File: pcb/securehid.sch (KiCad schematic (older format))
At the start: 194 parts, among them J1 USB_B_Micro, J2 SWD_HOST, J3 UART_HOST, J4 SWD_DEVICE, J5 UART_DEVICE, J6 USB_A, J7 USB_SPARE, J8 USB_A, Q1 AO3400, Q2 AO3400, Q3 AO3400, SW1 SW_Push, U1 AP1117-33, U2 STM32F103C8T6, U3 STM32F407VET6, U4 FE1.1s, U5 AP1117-33, Y1 8MHz, Y2 8MHz, Y3 32.768kHz, Y4 12MHz

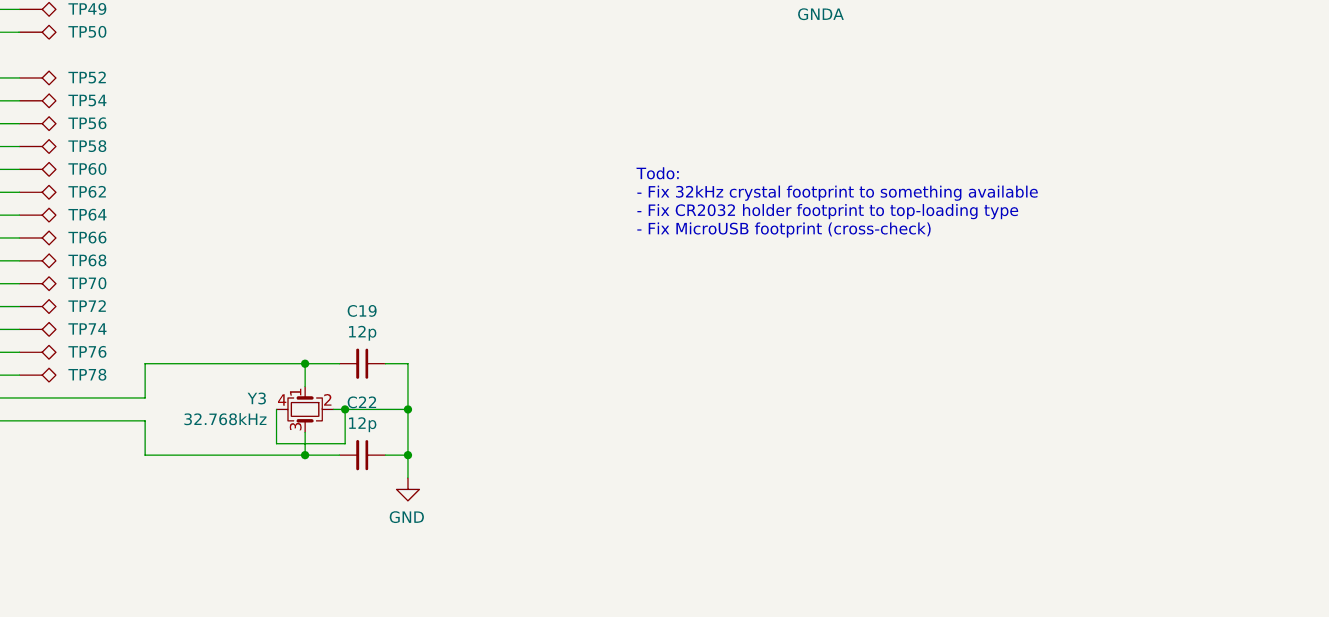
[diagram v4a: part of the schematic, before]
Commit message: Some small fixes, add silk artwork
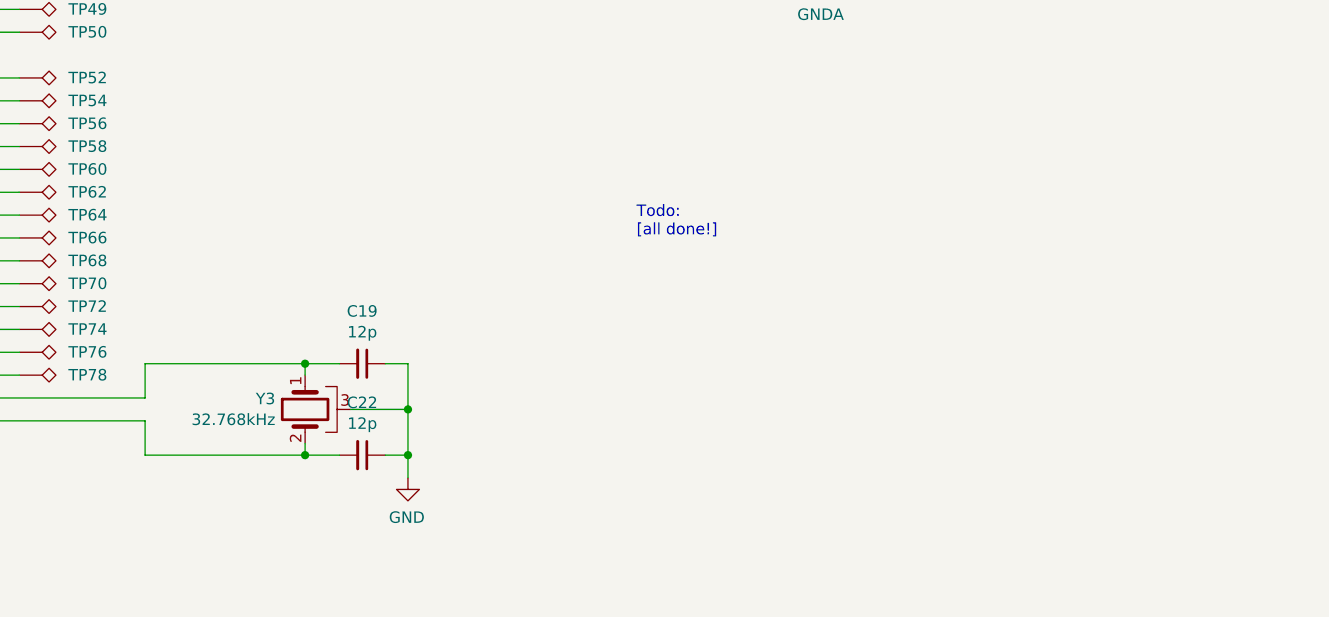
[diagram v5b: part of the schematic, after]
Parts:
- removed Y3: 32.768kHz, Crystal:Crystal_SMD_TXC_7M-4Pin_3.2x2.5mm, symbol device:Crystal_GND24_Small
- added Y3: 32.768kHz, Crystal:Crystal_C26-LF_D2.1mm_L6.5mm_Horizontal_1EP_style1, symbol Device:Crystal_GND3
- BT1: footprint Battery:BatteryHolder_MPD_BC2003_1x2032 -> Battery:BatteryHolder_Keystone_1060_1x2032
- J1: footprint Connector_USB:USB_Micro-B_GCT_USB3076-30-A -> footprints:microusb_ali_dovetail
- Y1, Y2, Y4: footprint Crystal:Crystal_SMD_TXC_7M-4Pin_3.2x2.5mm -> Crystal:Crystal_SMD_TXC_7M-4Pin_3.2x2.5mm_HandSoldering
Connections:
- net GND: now also Y3.3
- net at C19.2, U3.8 (PC14): now also Y3.1
- net at C22.2, U3.9 (PC15): now also Y3.2
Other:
- note added: "Todo:\n[all done!]"
- note removed: "Todo:\n- Fix 32kHz crystal footprint to something available\n- Fix CR2032 holder footprint to top-loading type\n- Fix MicroUSB footprint (cross-check)"
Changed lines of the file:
@@
 F 0 "J1" H 1500 4400 50  0000 L CNN
 F 1 "USB_B_Micro" H 1500 4300 50  0000 L CNN
-F 2 "Connector_USB:USB_Micro-B_GCT_USB3076-30-A" H 1850 3900 50  0001 C CNN
+F 2 "footprints:microusb_ali_dovetail" H 1850 3900 50  0001 C CNN
 F 3 "" H 1850 3900 50  0001 C CNN
 	1    1700 3950
@@
 F 0 "Y2" V 6554 3816 50  0000 L CNN
 F 1 "8MHz" V 6645 3816 50  0000 L CNN
-F 2 "Crystal:Crystal_SMD_TXC_7M-4Pin_3.2x2.5mm" H 6600 3650 50  0001 C CNN
+F 2 "Crystal:Crystal_SMD_TXC_7M-4Pin_3.2x2.5mm_HandSoldering" H 6600 3650 50  0001 C CNN
 F 3 "" H 6600 3650 50  0001 C CNN
 	1    6600 3650
@@
 F 0 "BT1" H 7500 1750 50  0000 L CNN
 F 1 "CR2032" H 7300 1650 50  0000 L CNN
-F 2 "Battery:BatteryHolder_MPD_BC2003_1x2032" V 7750 1710 50  0001 C CNN
+F 2 "Battery:BatteryHolder_Keystone_1060_1x2032" V 7750 1710 50  0001 C CNN
 F 3 "" V 7750 1710 50  0001 C CNN
 	1    7750 1650
@@
 F 0 "Y4" V 1954 7266 50  0000 L CNN
 F 1 "12MHz" V 2045 7266 50  0000 L CNN
-F 2 "Crystal:Crystal_SMD_TXC_7M-4Pin_3.2x2.5mm" H 2000 7100 50  0001 C CNN
+F 2 "Crystal:Crystal_SMD_TXC_7M-4Pin_3.2x2.5mm_HandSoldering" H 2000 7100 50  0001 C CNN
 F 3 "" H 2000 7100 50  0001 C CNN
 	1    2000 7100
@@
 F 0 "Y1" V 11154 2866 50  0000 L CNN
 F 1 "8MHz" V 11245 2866 50  0000 L CNN
-F 2 "Crystal:Crystal_SMD_TXC_7M-4Pin_3.2x2.5mm" H 11200 2700 50  0001 C CNN
+F 2 "Crystal:Crystal_SMD_TXC_7M-4Pin_3.2x2.5mm_HandSoldering" H 11200 2700 50  0001 C CNN
 F 3 "" H 11200 2700 50  0001 C CNN
 	1    11200 2700
@@
 SECURE_IF_F4TX
 $Comp
-L device:Crystal_GND24_Small Y3
-U 1 1 5C1E1737
-P 10700 7050
-F 0 "Y3" V 10654 7216 50  0000 L CNN
-F 1 "32.768kHz" V 10745 7216 50  0000 L CNN
-F 2 "Crystal:Crystal_SMD_TXC_7M-4Pin_3.2x2.5mm" H 10700 7050 50  0001 C CNN
-F 3 "" H 10700 7050 50  0001 C CNN
-	1    10700 7050
-	0    -1   1    0
-$EndComp
-$Comp
 L device:C_Small C19
 U 1 1 5C1E173E
@@
 	10850 6850 10700 6850
 Wire Wire Line
-	10700 6850 10700 6950
+	10700 6850 10700 6900
 Connection ~ 10700 6850
 Wire Wire Line
@@
 Wire Wire Line
 	10000 7100 9350 7100
-Wire Wire Line
-	10700 7150 10700 7250
 Connection ~ 10700 7250
 Wire Wire Line
-	11150 6850 11150 7050
-Wire Wire Line
 	11150 7250 11050 7250
 Wire Wire Line
@@
 Connection ~ 11150 7250
 Wire Wire Line
-	10825 7050 10875 7050
-Connection ~ 11150 7050
-Wire Wire Line
-	11150 7050 11150 7250
-Wire Wire Line
-	10575 7050 10575 7200
-Wire Wire Line
-	10575 7200 10875 7200
-Wire Wire Line
-	10875 7200 10875 7050
-Connection ~ 10875 7050
-Wire Wire Line
-	10875 7050 11150 7050
-Wire Wire Line
 	10000 6850 10700 6850
 Wire Wire Line
@@
 $EndComp
 Text Notes 12150 6300 0    50   ~ 0
-Todo:\n- Fix 32kHz crystal footprint to something available\n- Fix CR2032 holder footprint to top-loading type\n- Fix MicroUSB footprint (cross-check)
+Todo:\n[all done!]
 Connection ~ 7950 10750
+Wire Wire Line
+	10700 7200 10700 7250
+$Comp
+L Device:Crystal_GND3 Y3
+U 1 1 5C2565BB
+P 10700 7050
+F 0 "Y3" V 10654 7180 50  0000 L CNN
+F 1 "32.768kHz" V 10745 7180 50  0000 L CNN
+F 2 "Crystal:Crystal_C26-LF_D2.1mm_L6.5mm_Horizontal_1EP_style1" H 10700 7050 50  0001 C CNN
+F 3 "~" H 10700 7050 50  0001 C CNN
+	1    10700 7050
+	0    -1   1    0
+$EndComp
+Wire Wire Line
+	11150 6850 11150 7050
+Wire Wire Line
+	10900 7050 11150 7050
+Connection ~ 11150 7050
+Wire Wire Line
+	11150 7050 11150 7250
 $EndSCHEMATC

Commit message: Make a really fancy diagram
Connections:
- net GND: now also Q2.2 (S); no longer Q2.3 (D)
- net at R18.2, R19.2, R20.2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: now also Q2.3 (D); no longer Q2.2 (S)
- no-connect marks 3 -> 4
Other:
- note added: "Todo:\nConsider flipping some components to match top-mount case\nUSB hub chip doesn't work and gets warm\nQ1 or Q2 wasn't oriented correctly. Fixed in schematic, needs to be fixed in PCB"
- note removed: "Todo:\n[all done!]"
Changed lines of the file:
@@
 F 3 "https://www.fairchildsemi.com/datasheets/2N/2N7002.pdf" H 11650 9700 50  0001 L CNN
 	1    11650 9700
-	-1   0    0    1
+	-1   0    0    -1
 $EndComp
 $Comp
@@
 $EndComp
 Text Notes 12150 6300 0    50   ~ 0
-Todo:\n[all done!]
+Todo:\nConsider flipping some components to match top-mount case\nUSB hub chip doesn't work and gets warm\nQ1 or Q2 wasn't oriented correctly. Fixed in schematic, needs to be fixed in PCB
 Connection ~ 7950 10750
 Wire Wire Line
@@
 Wire Wire Line
 	11150 7050 11150 7250
+NoConn ~ 1950 400
 $EndSCHEMATC
